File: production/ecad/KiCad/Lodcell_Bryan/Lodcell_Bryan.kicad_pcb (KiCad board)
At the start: 4 copper layers, 50.7 x 25.1 mm, 23 parts, among them J1 LoadCellConnector, J2 power_for_Loadcell, J3 ConnToESP32, U3 ADS1231IDR, U4 TXB0104DR

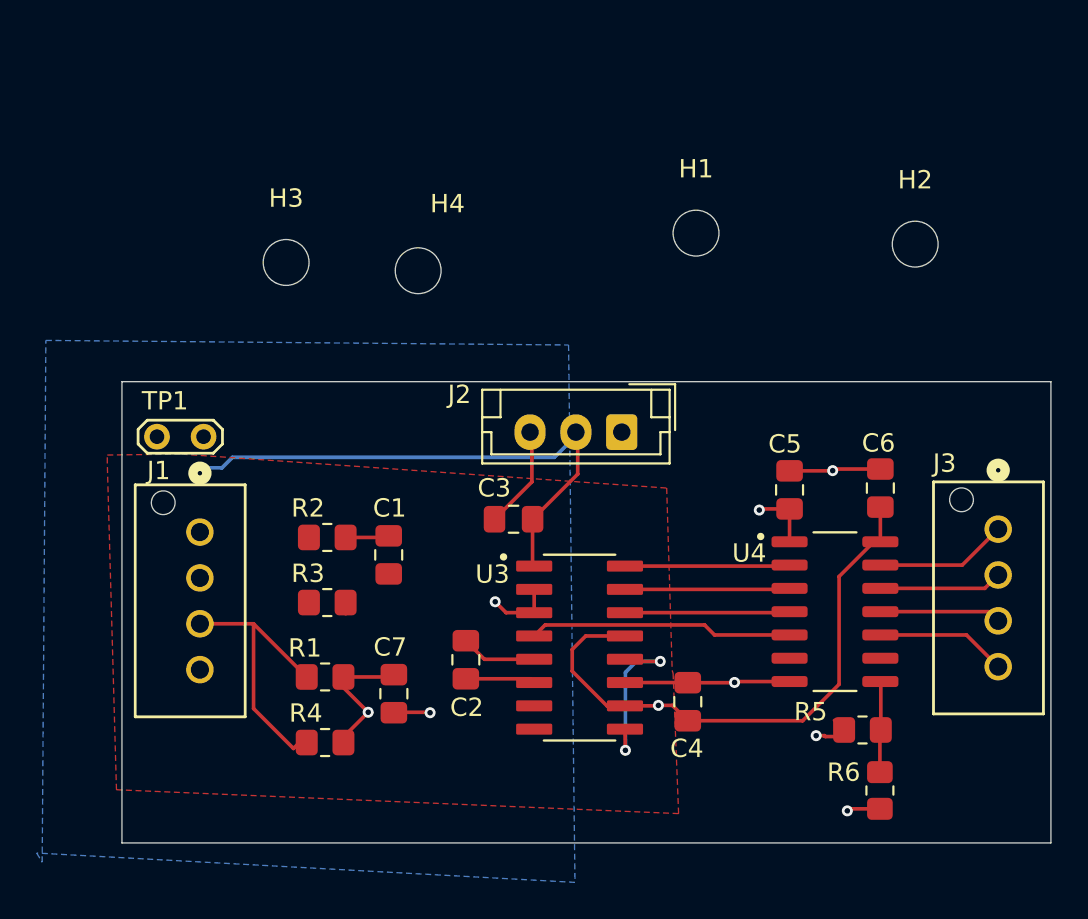
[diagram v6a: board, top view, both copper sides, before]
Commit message: Added DOUT test point
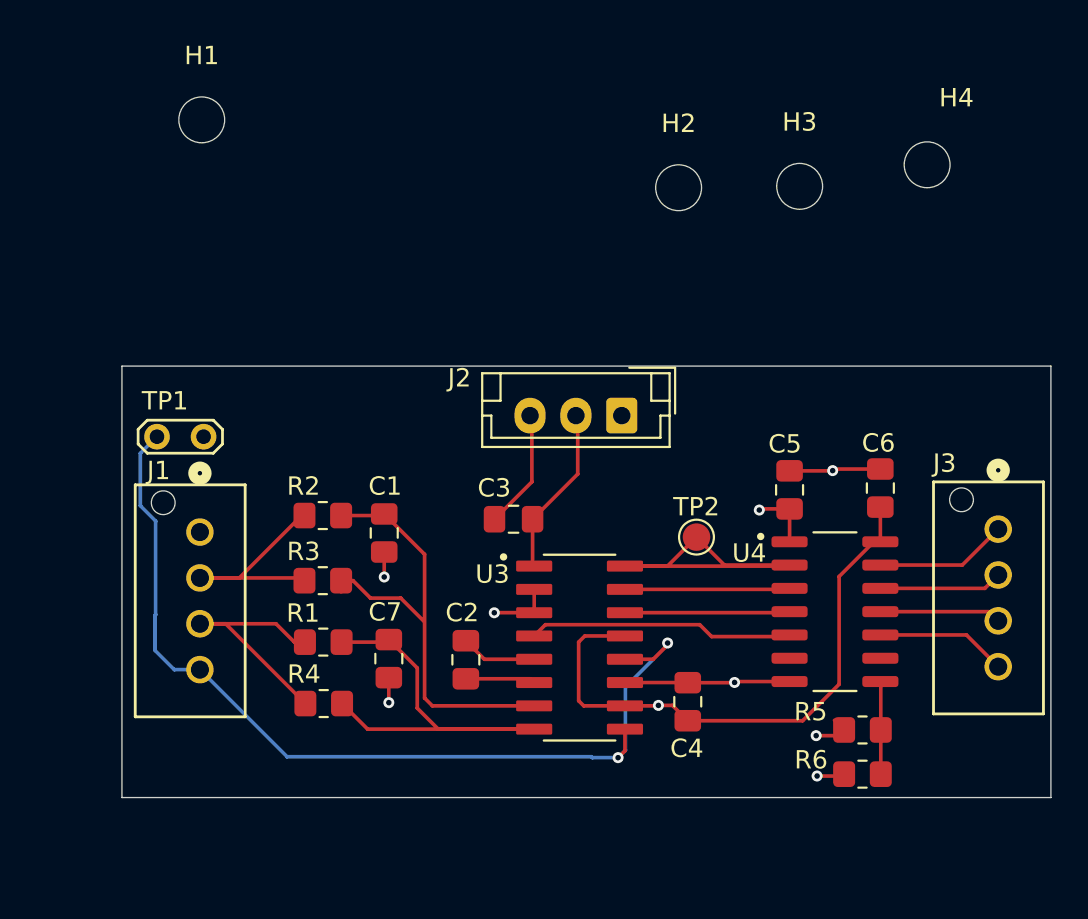
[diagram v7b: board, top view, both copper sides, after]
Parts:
- added TP2: TestPad_DOUT, TestPoint:TestPoint_Pad_D1.5mm, F.Cu at (178.2, 60.9)
- moved H4 28.3 mm to (190.8, 40.6)
- moved H3 28.3 mm to (183.8, 41.8)
- moved H1 27.6 mm to (151.2, 38.1)
- moved H2 13.3 mm to (177.2, 41.8)
- moved R4 2.13 mm to (157.8, 70.0)
- moved C7 1.93 mm to (161.4, 67.5)
- moved R1 1.90 mm to (157.8, 66.6)
- moved R6 1.30 mm to (187.2, 73.8), turned to 180 degrees
- moved C1 1.22 mm to (161.2, 60.6)
- moved R2 1.22 mm to (157.8, 59.7)
- moved R3 1.22 mm to (157.8, 63.2)
- moved J2 0.90 mm to (174.1, 54.2)
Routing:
- net Net-(J1-Pin_4): track 9.65 -> 52.2 mm
- net /LP_+: track 3.18 -> 25.7 mm
- net +5V: track 61.1 -> 40.4 mm
- net /LP_-: track 7.70 -> 26.0 mm, vias 1 -> 0
- net /RawLoadCell_+: track 0.16 -> 12.9 mm
- net Net-(U3-~{DRDY}/DOUT): track 9.00 -> 19.3 mm
- net /RawLoadCell_-: track 15.6 -> 14.1 mm
- net GND: track 27.5 -> 28.2 mm, vias 5 -> 6
- removed copper zone on B.Cu, net /LP_-
- removed copper zone on F.Cu, net Net-(J1-Pin_4)
- removed copper zone on In2.Cu, net Net-(J1-Pin_4)
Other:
- board size 50.7 x 25.1 mm -> 50.7 x 23.5 mm

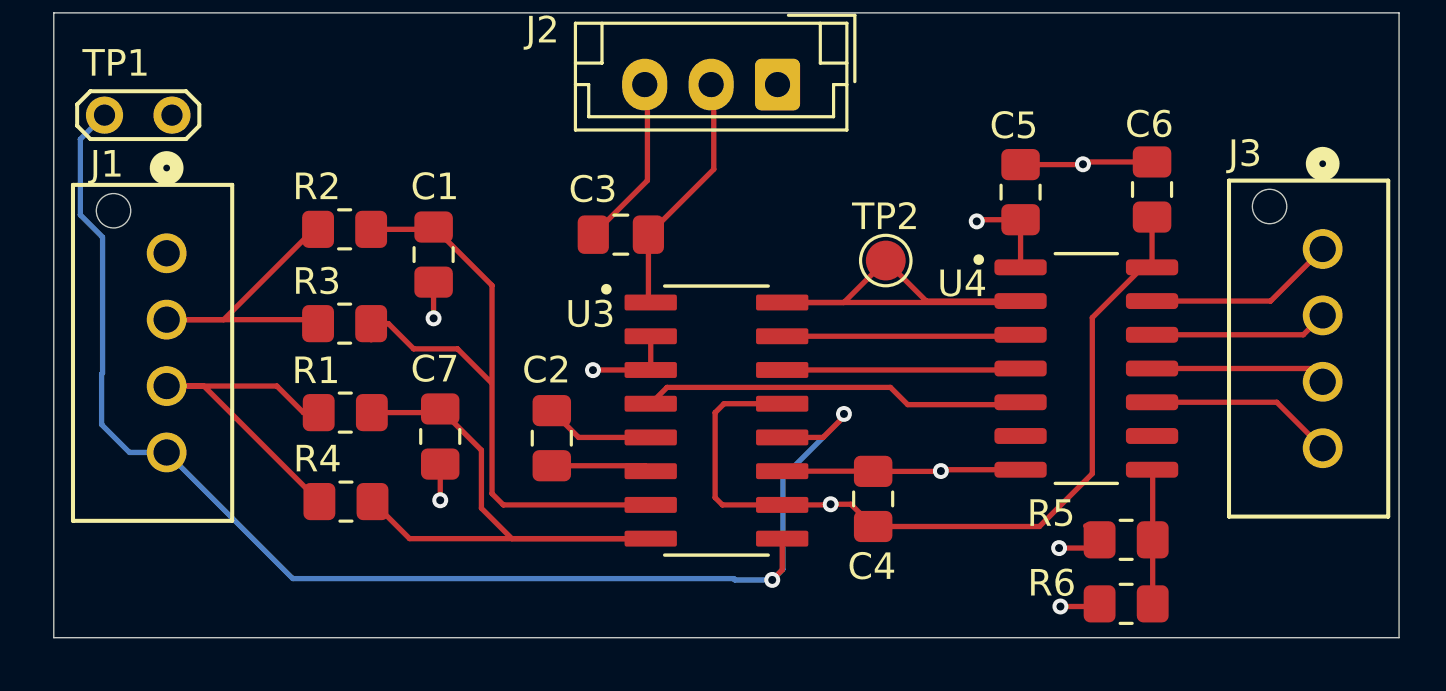
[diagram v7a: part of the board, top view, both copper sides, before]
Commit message: Improved diff. load cell signals
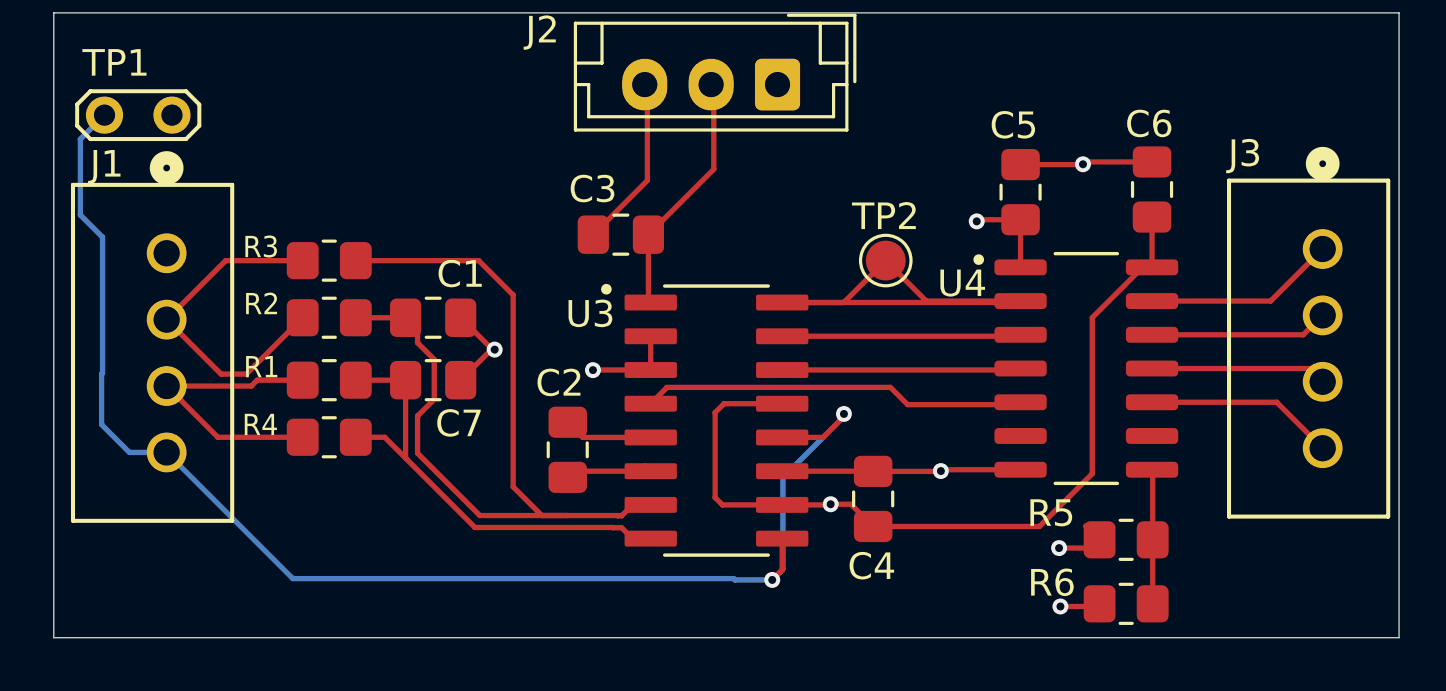
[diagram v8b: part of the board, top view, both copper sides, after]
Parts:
- moved R2 3.38 mm to (157.2, 63.0)
- moved R4 2.50 mm to (157.2, 67.5)
- moved R3 2.44 mm to (157.2, 60.9)
- moved C1 2.38 mm to (161.1, 63.0), turned to 0 degrees
- moved C7 2.14 mm to (161.1, 65.4), turned to 180 degrees
- moved R1 1.36 mm to (157.2, 65.4)
- moved C2 0.74 mm to (166.2, 68.0)
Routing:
- net /LP_-: track 26.0 -> 17.5 mm
- net /LP_+: track 25.7 -> 33.8 mm
- net /RawLoadCell_-: track 14.1 -> 11.1 mm
- net GND: track 28.2 -> 29.0 mm, vias 6 -> 5
- net Net-(U3-CAP1): track 4.14 -> 3.36 mm
